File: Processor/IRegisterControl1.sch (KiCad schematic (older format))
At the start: 12 parts

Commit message: Decoder 1 Rev 1
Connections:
- net ~MEM.RD renamed ~IMM_RD
- net ~MEM.WR renamed ~IMM_WR
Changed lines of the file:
@@
 $EndComp
 Text HLabel 5550 4450 2    50   Output ~ 0
-~MEM.RD
+~IMM_RD
 Text HLabel 5550 4650 2    50   Output ~ 0
 ~RH.RD
@@
 NoConn ~ 5450 5250
 Text HLabel 5650 6300 2    50   Output ~ 0
-~MEM.WR
+~IMM_WR
 Text HLabel 5550 6500 2    50   Output ~ 0
 ~RL.WR

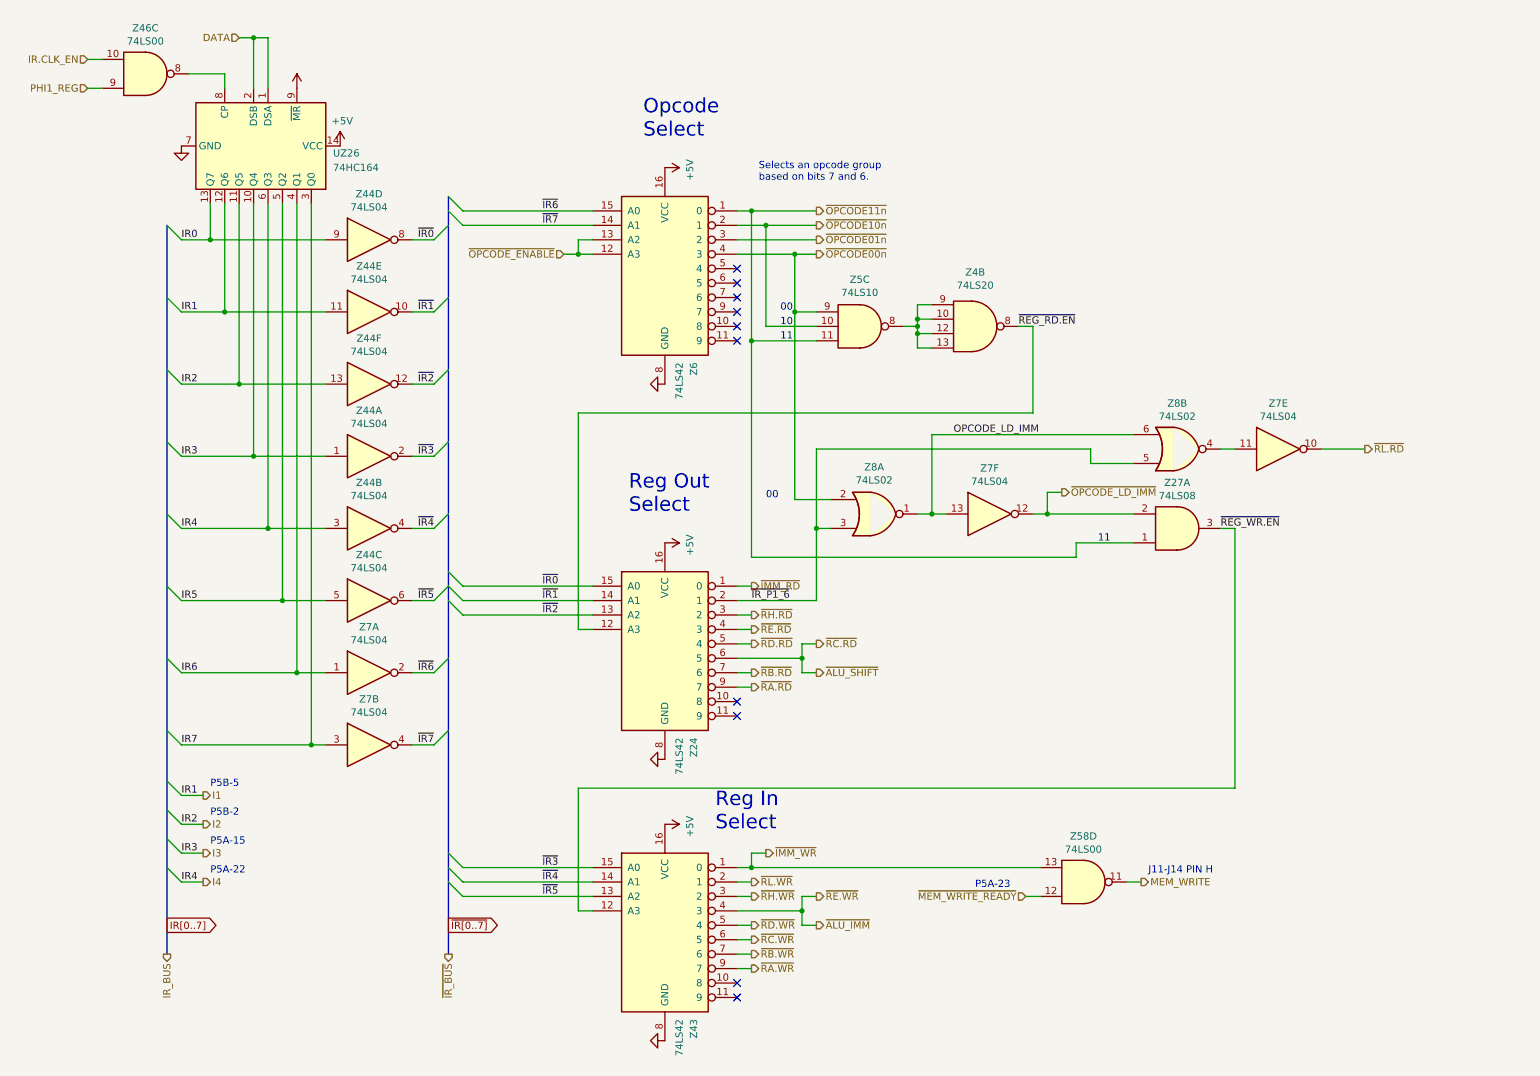
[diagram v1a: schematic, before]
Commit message: Schematics for display & keyboard, adding LEDs to processor PCB
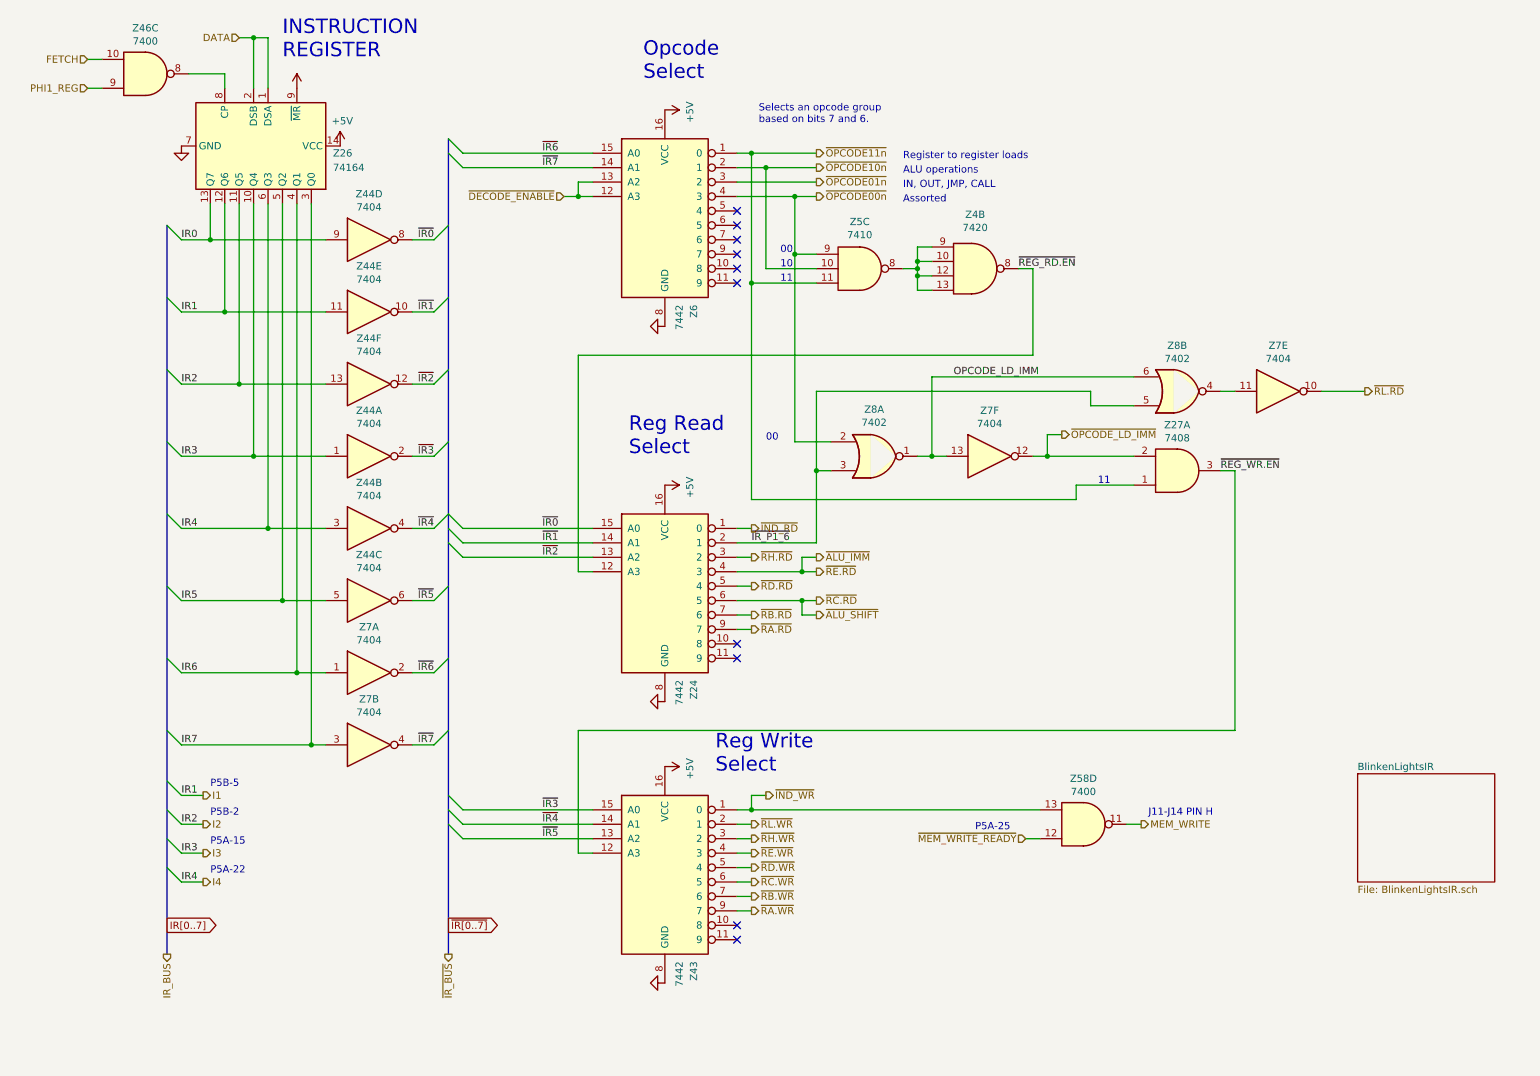
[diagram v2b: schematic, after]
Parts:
- Z24, Z43, Z6: value 74LS42 -> 7442; footprint (none) -> Package_DIP:DIP-16_W7.62mm_Socket
- Z26: renamed from UZ26; value 74HC164 -> 74164; footprint (none) -> Package_DIP:DIP-14_W7.62mm_Socket
- Z27: value 74LS08 -> 7408; footprint (none) -> Package_DIP:DIP-14_W7.62mm_Socket
- Z4: value 74LS20 -> 7420; footprint (none) -> Package_DIP:DIP-14_W7.62mm_Socket
- Z44, Z7: value 74LS04 -> 7404; footprint (none) -> Package_DIP:DIP-14_W7.62mm_Socket
- Z46, Z58: value 74LS00 -> 7400; footprint (none) -> Package_DIP:DIP-14_W7.62mm_Socket
- Z5: value 74LS10 -> 7410; footprint (none) -> Package_DIP:DIP-14_W7.62mm_Socket
- Z8: value 74LS02 -> 7402; footprint (none) -> Package_DIP:DIP-14_W7.62mm_Socket
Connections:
- net ~RE.RD is gone; now on net ~ALU_IMM: Z24.4 (3)
- net ~ALU_IMM: no longer Z43.4 (3)
- net IR.CLK_EN renamed FETCH
- net ~IMM_RD renamed ~IND_RD
- net ~IMM_WR renamed ~IND_WR
- net ~OPCODE_ENABLE renamed ~DECODE_ENABLE
- new net ~RE.WR: Z43.4 (3)
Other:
- note added: "ALU operations"
- note added: "Assorted"
- note added: "IN, OUT, JMP, CALL"
- note added: "INSTRUCTION\nREGISTER"
- note added: "P5A-25"
- note added: "Reg Read\nSelect"
- note added: "Reg Write\nSelect"
- note added: "Register to register loads"
- note removed: "P5A-23"
- note removed: "Reg In\nSelect"
- note removed: "Reg Out\nSelect"
- moved on the sheet: Z24, Z27A, Z43, Z4B, Z58D, Z5C, Z6, Z7E, Z7F, Z8A, Z8B
